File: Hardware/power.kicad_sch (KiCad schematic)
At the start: 10 parts, among them U2 ADP2164ACPZ-3.3-R7

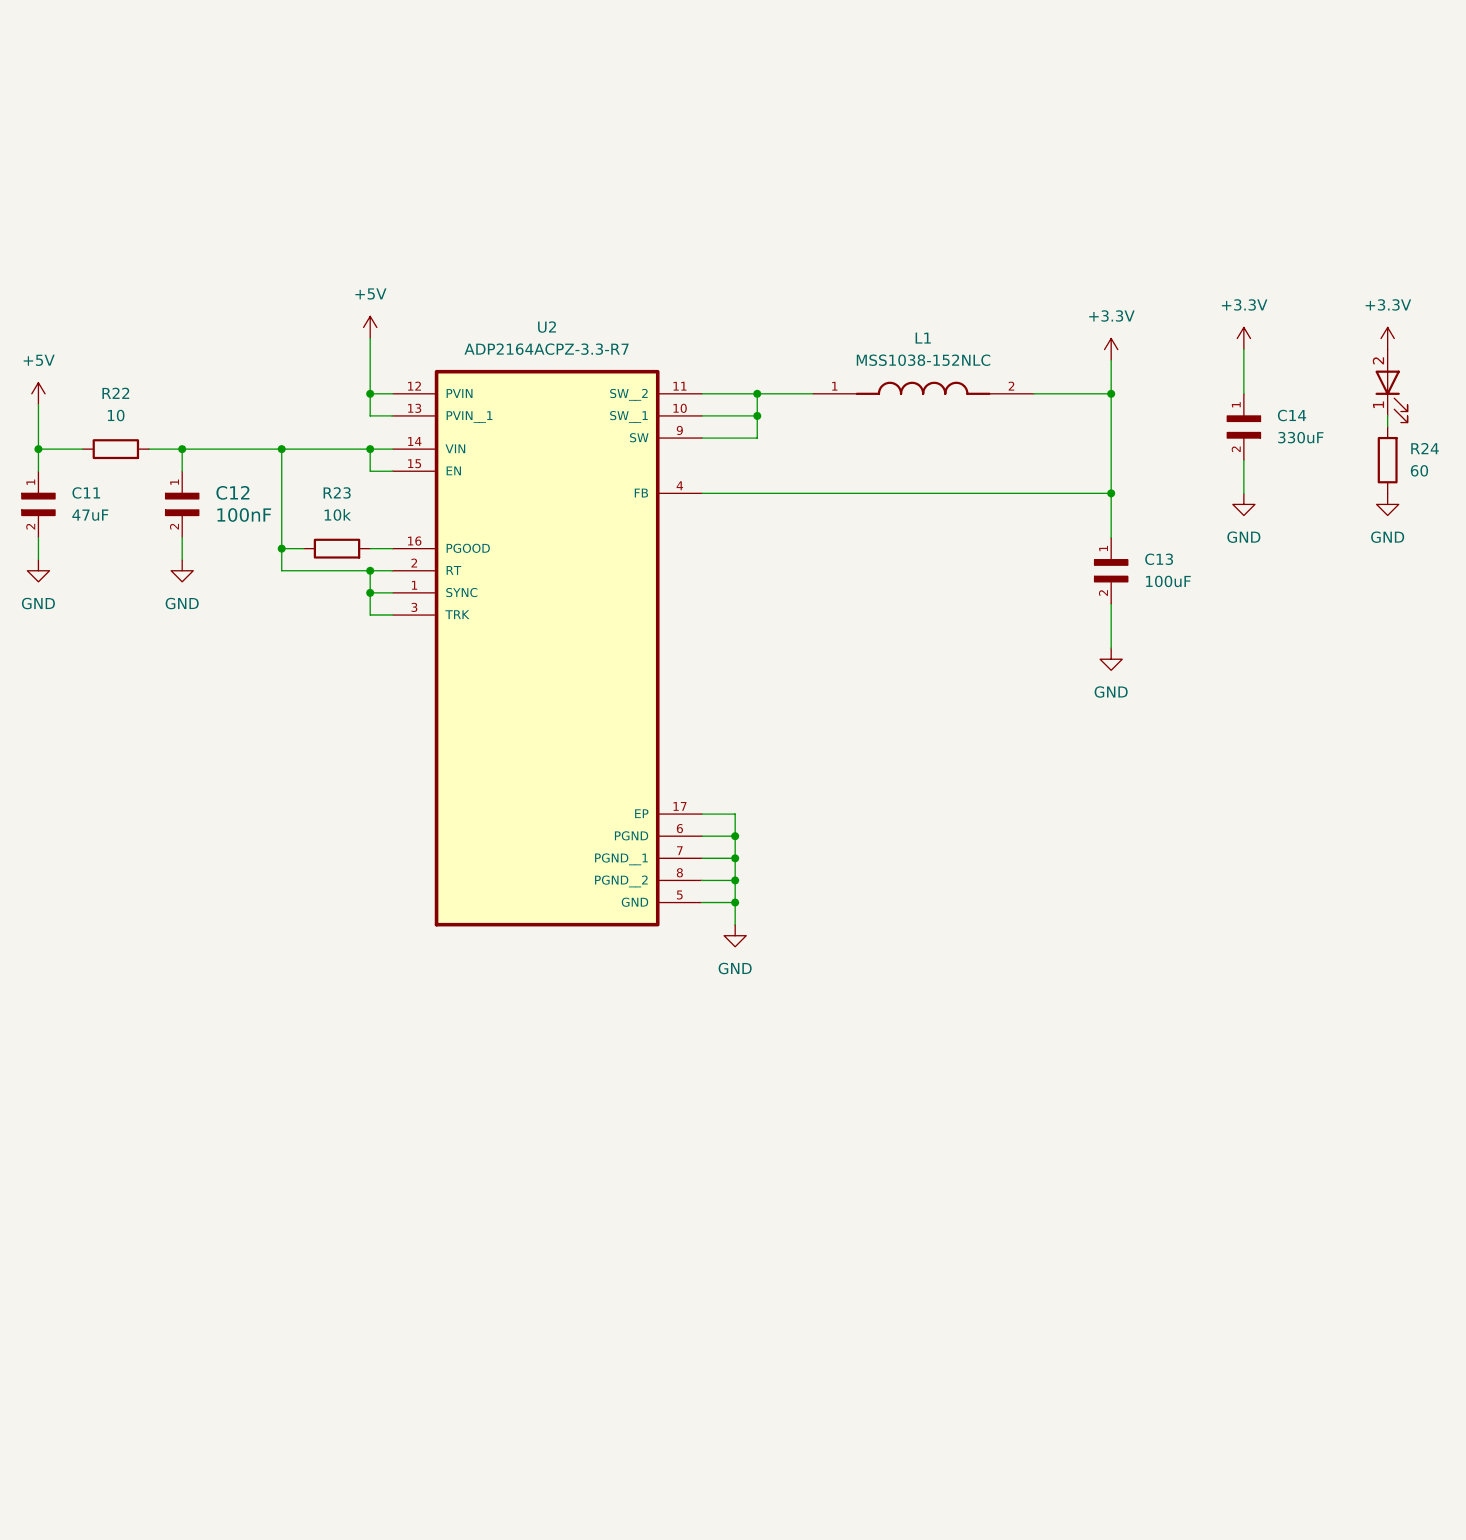
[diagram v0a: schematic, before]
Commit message: Added oscillators, reset button, and finalized ETH connection
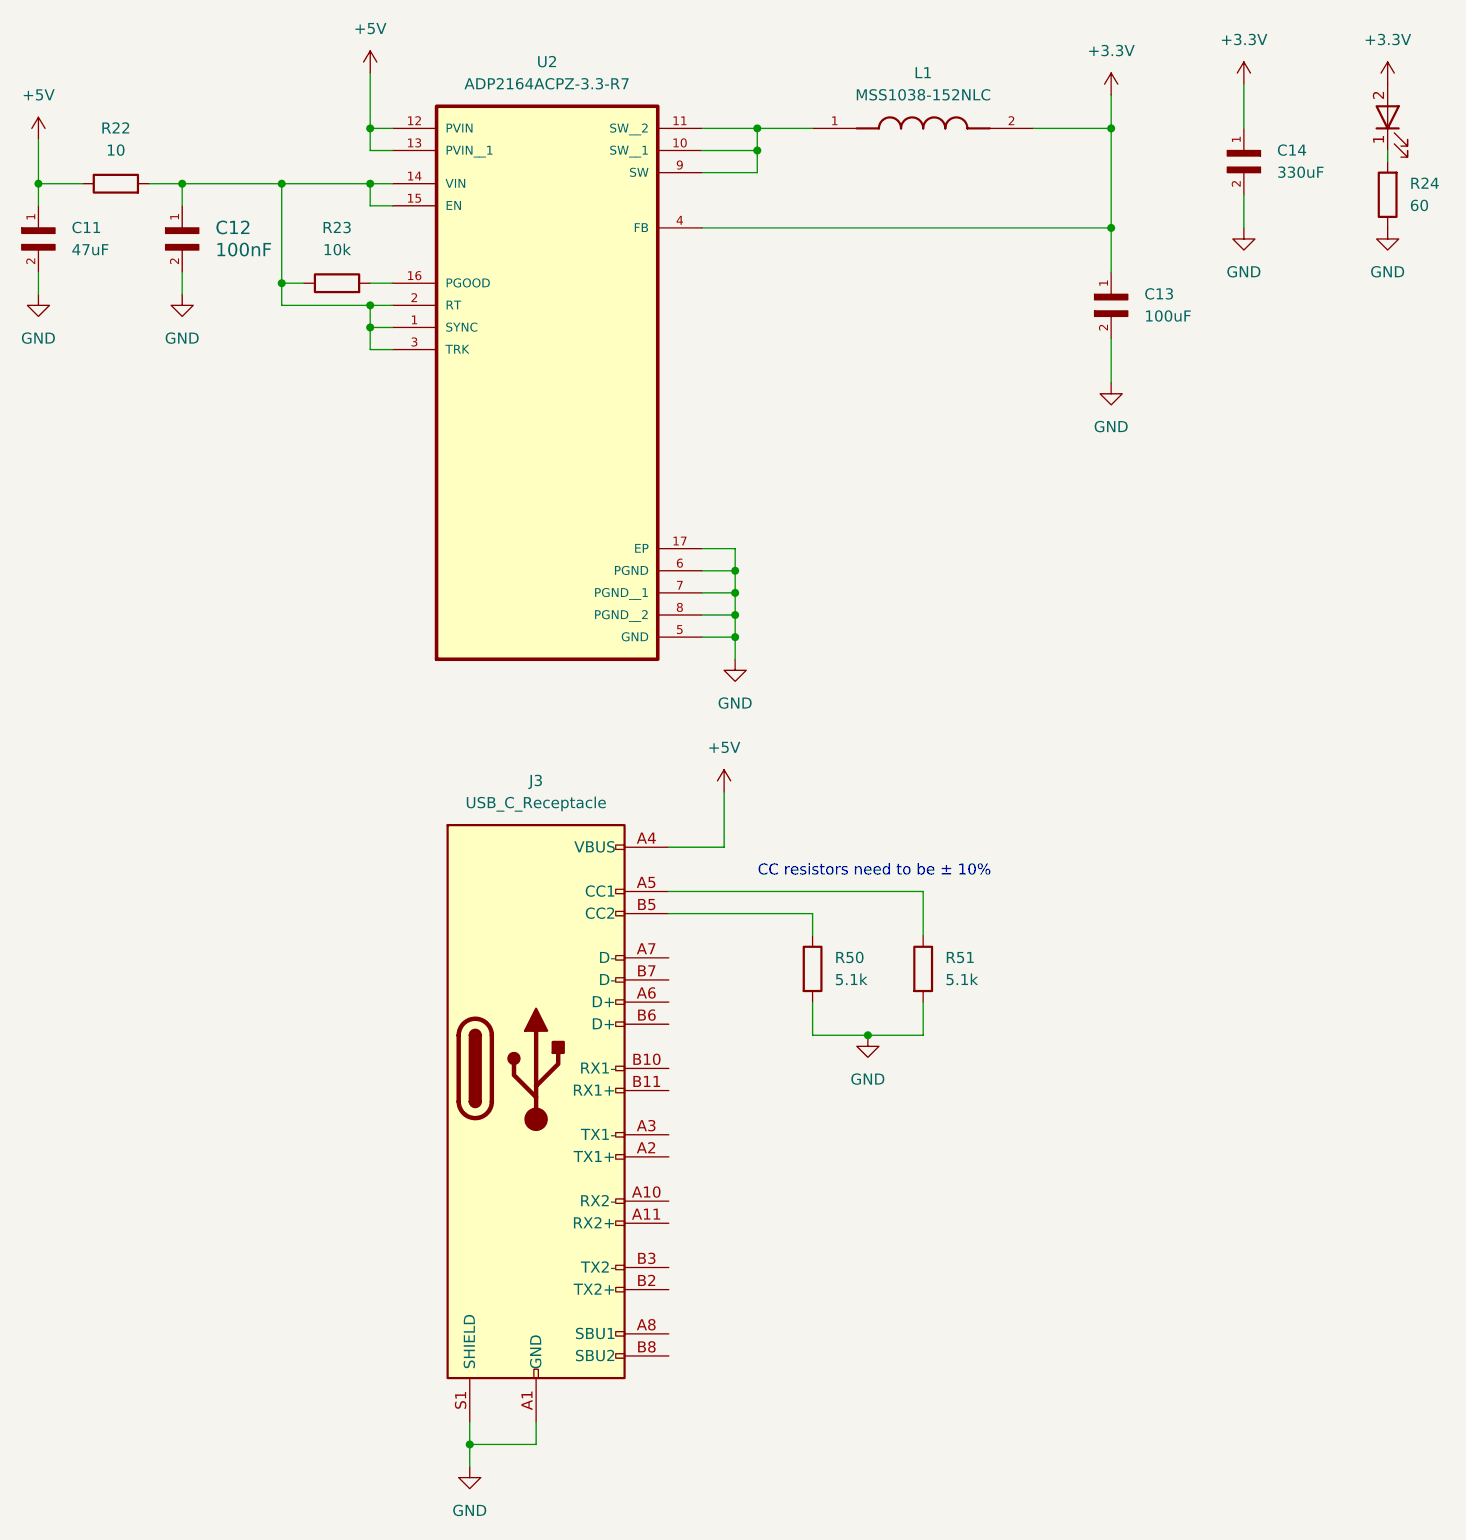
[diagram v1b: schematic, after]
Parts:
- added J3: USB_C_Receptacle, Connector_USB:USB_C_Receptacle_Amphenol_12401548E4-2A, symbol Connector:USB_C_Receptacle
- added R50, R51: 5.1k, Resistor_SMD:R_0402_1005Metric, symbol Device:R
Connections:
- net +5V: now also J3.A4 (VBUS), J3.A9 (VBUS), J3.B4 (VBUS), J3.B9 (VBUS)
- net GND: now also J3.A1 (GND), J3.A12 (GND), J3.B1 (GND), J3.B12 (GND), J3.S1 (SHIELD), R50.2, R51.2
- new net: J3.B5 (CC2), R50.1
- new net: J3.A5 (CC1), R51.1
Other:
- note added: "CC resistors need to be ± 10%"
- moved on the sheet: C11, C12, C13, C14, L1, R22, R23, R24, U2
